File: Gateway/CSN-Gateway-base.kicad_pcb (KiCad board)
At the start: 2 copper layers, 32 x 85.5 mm, 51 parts, among them IC1 ATMEGA328-A, P2 CONN4, P3 CONN_ICSP, P5 CONN6, P8 CONN_NRF24L01, Q1 2N2222, U1 MAX485CSA, U2 AMS1117-3.3V, U3 ATSHA204A, Y1 Crystal

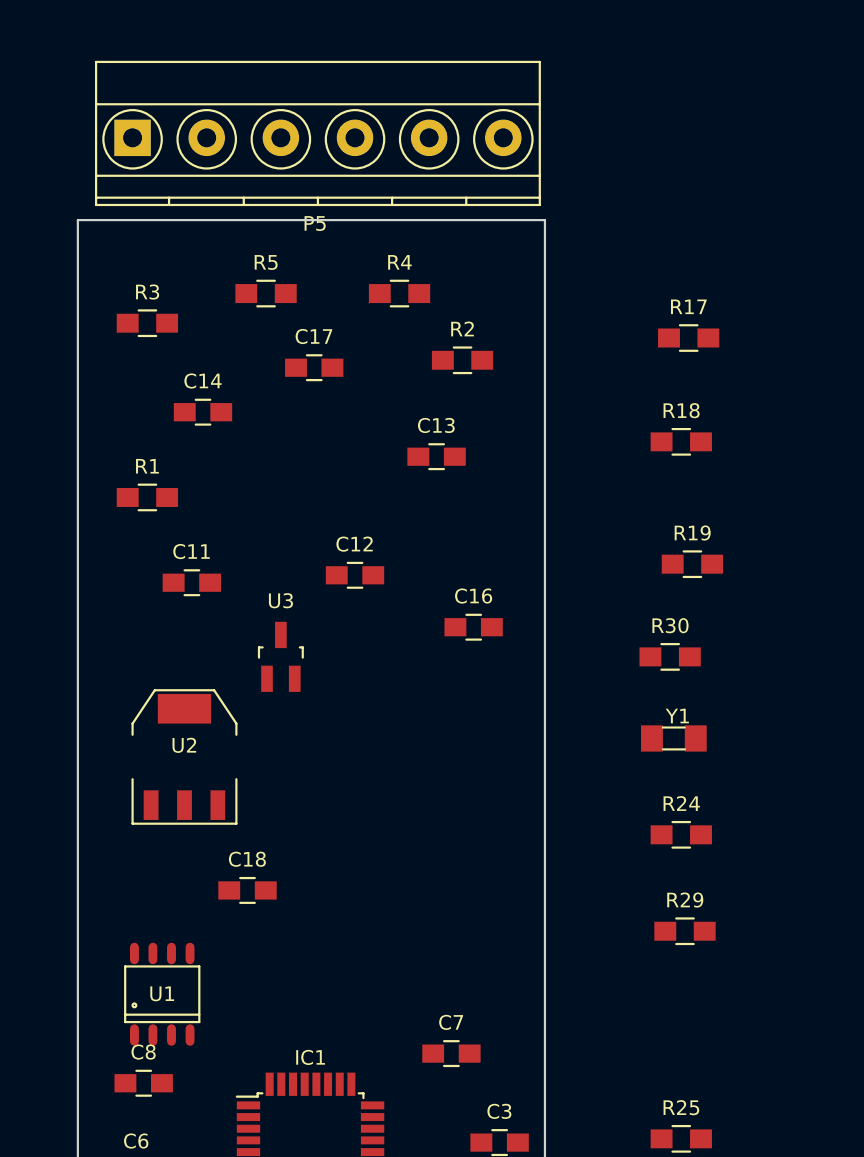
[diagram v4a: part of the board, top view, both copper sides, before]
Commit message: add all missing footprints
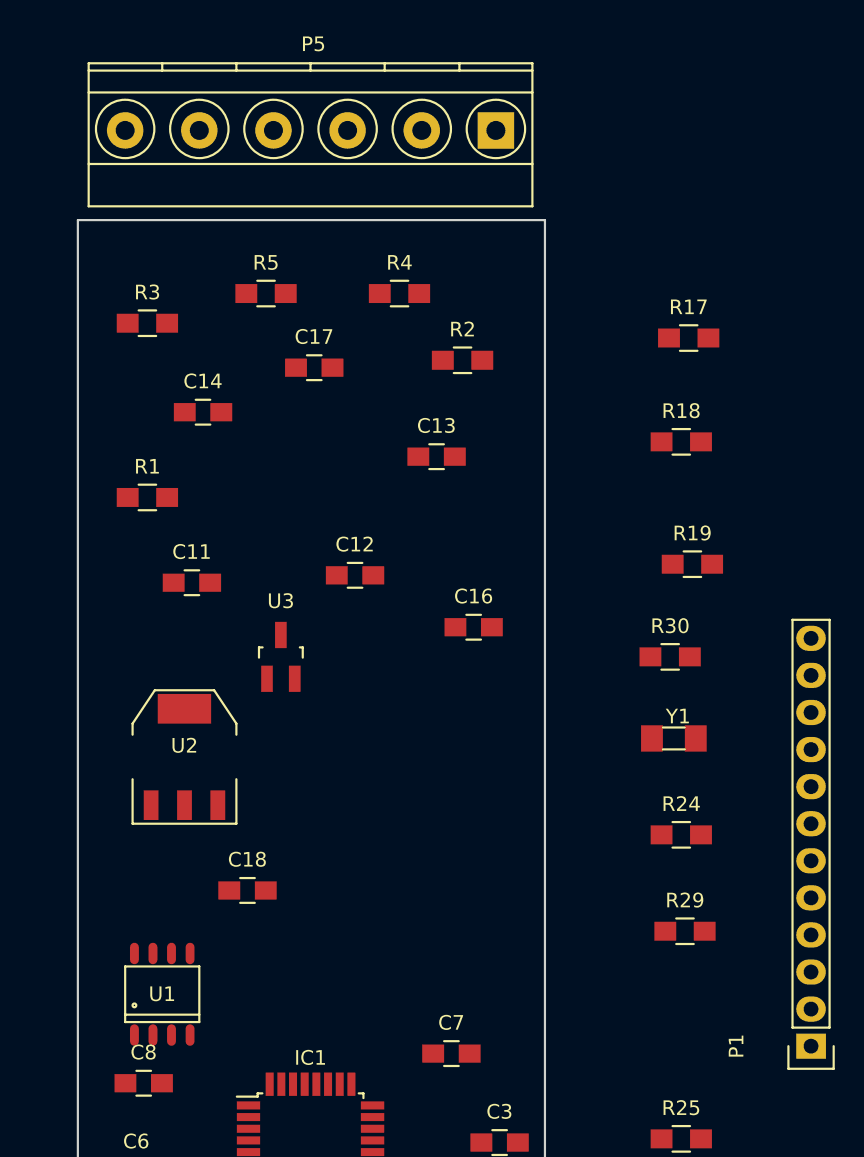
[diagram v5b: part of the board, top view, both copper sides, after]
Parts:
- added P1: CONN_02X06, Socket_Strips:Socket_Strip_Straight_1x12, F.Cu at (189.2, 117.1)
- moved P5 24.9 mm to (167.6, 54.4), turned to 180 degrees
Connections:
- IC1 pad 10: (no net) -> RGB2
- IC1 pad 11: (no net) -> RGB3
- IC1 pad 12: (no net) -> BTN1
- IC1 pad 25: (no net) -> BTN2
- IC1 pad 26: (no net) -> RGB1
- IC1 pad 28: (no net) -> SCL
- IC1 pad 30: (no net) -> RXI
- IC1 pad 31: (no net) -> TXO
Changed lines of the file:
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@@
 (kicad_pcb (version 4) (host pcbnew 4.0.4-stable)
   (general
-    (links 122)
-    (no_connects 122)
+    (links 134)
+    (no_connects 134)
     (area 138.924999 60.424999 171.075001 146.075001)
     (thickness 1.6)
@@
     (tracks 0)
     (zones 0)
-    (modules 51)
-    (nets 31)
+    (modules 52)
+    (nets 39)
   )
   (page A4)
@@
   (net 29 RS485-A)
   (net 30 RS485-B)
+  (net 31 RGB2)
+  (net 32 RGB3)
+  (net 33 BTN1)
+  (net 34 BTN2)
+  (net 35 RGB1)
+  (net 36 SCL)
+  (net 37 RXI)
+  (net 38 TXO)
   (net_class Default "Ceci est la Netclass par défaut"
     (clearance 0.2)
@@
     (add_net A2)
     (add_net A3)
+    (add_net BTN1)
+    (add_net BTN2)
     (add_net CE)
     (add_net CSN)
@@
     (add_net "Net-(D2-Pad1)")
     (add_net "Net-(P2-Pad2)")
+    (add_net RGB1)
+    (add_net RGB2)
+    (add_net RGB3)
     (add_net RS485-A)
     (add_net RS485-B)
@@
     (add_net RS485_TX)
     (add_net RST)
+    (add_net RXI)
     (add_net SCK)
+    (add_net SCL)
     (add_net SDA)
+    (add_net TXO)
     (add_net VCC)
   )
@@
     (pad 9 smd rect (at -2.8 4.25 90) (size 1.6 0.55) (layers F.Cu F.Paste F.Mask)
       (net 15 RS485_EN))
-    (pad 10 smd rect (at -2 4.25 90) (size 1.6 0.55) (layers F.Cu F.Paste F.Mask))
-    (pad 11 smd rect (at -1.2 4.25 90) (size 1.6 0.55) (layers F.Cu F.Paste F.Mask))
-    (pad 12 smd rect (at -0.4 4.25 90) (size 1.6 0.55) (layers F.Cu F.Paste F.Mask))
+    (pad 10 smd rect (at -2 4.25 90) (size 1.6 0.55) (layers F.Cu F.Paste F.Mask)
+      (net 31 RGB2))
+    (pad 11 smd rect (at -1.2 4.25 90) (size 1.6 0.55) (layers F.Cu F.Paste F.Mask)
+      (net 32 RGB3))
+    (pad 12 smd rect (at -0.4 4.25 90) (size 1.6 0.55) (layers F.Cu F.Paste F.Mask)
+      (net 33 BTN1))
     (pad 13 smd rect (at 0.4 4.25 90) (size 1.6 0.55) (layers F.Cu F.Paste F.Mask)
       (net 22 CE))
@@
     (pad 24 smd rect (at 4.25 -2.8) (size 1.6 0.55) (layers F.Cu F.Paste F.Mask)
       (net 18 A1))
-    (pad 25 smd rect (at 2.8 -4.25 90) (size 1.6 0.55) (layers F.Cu F.Paste F.Mask))
-    (pad 26 smd rect (at 2 -4.25 90) (size 1.6 0.55) (layers F.Cu F.Paste F.Mask))
+    (pad 25 smd rect (at 2.8 -4.25 90) (size 1.6 0.55) (layers F.Cu F.Paste F.Mask)
+      (net 34 BTN2))
+    (pad 26 smd rect (at 2 -4.25 90) (size 1.6 0.55) (layers F.Cu F.Paste F.Mask)
+      (net 35 RGB1))
     (pad 27 smd rect (at 1.2 -4.25 90) (size 1.6 0.55) (layers F.Cu F.Paste F.Mask)
       (net 19 SDA))
-    (pad 28 smd rect (at 0.4 -4.25 90) (size 1.6 0.55) (layers F.Cu F.Paste F.Mask))
+    (pad 28 smd rect (at 0.4 -4.25 90) (size 1.6 0.55) (layers F.Cu F.Paste F.Mask)
+      (net 36 SCL))
     (pad 29 smd rect (at -0.4 -4.25 90) (size 1.6 0.55) (layers F.Cu F.Paste F.Mask)
       (net 3 RST))
-    (pad 30 smd rect (at -1.2 -4.25 90) (size 1.6 0.55) (layers F.Cu F.Paste F.Mask))
-    (pad 31 smd rect (at -2 -4.25 90) (size 1.6 0.55) (layers F.Cu F.Paste F.Mask))
+    (pad 30 smd rect (at -1.2 -4.25 90) (size 1.6 0.55) (layers F.Cu F.Paste F.Mask)
+      (net 37 RXI))
+    (pad 31 smd rect (at -2 -4.25 90) (size 1.6 0.55) (layers F.Cu F.Paste F.Mask)
+      (net 38 TXO))
     (pad 32 smd rect (at -2.8 -4.25 90) (size 1.6 0.55) (layers F.Cu F.Paste F.Mask)
       (net 28 IRQ))
@@
   )
   (module footprints:TerminalBlock_Multicomp-5-08-6pol (layer F.Cu)
-    (at 142.748 54.864)
+    (at 167.64 54.356 180)
     (descr "6-way 5.08mm pitch terminal block, Multicomp MC000038")
-    (fp_text reference P5 (at 12.5 5.9) (layer F.SilkS)
-      (effects (font (size 1 1) (thickness 0.15)))
-    )
-    (fp_text value CONN6 (at 12.5 -6.6) (layer F.Fab)
+    (fp_text reference P5 (at 12.5 5.9 180) (layer F.SilkS)
+      (effects (font (size 1 1) (thickness 0.15)))
+    )
+    (fp_text value CONN6 (at 12.5 -6.6 180) (layer F.Fab)
       (effects (font (size 1 1) (thickness 0.15)))
     )
@@
     (fp_line (start 27.9 -5.2) (end -2.5 -5.2) (layer F.SilkS) (width 0.15))
     (fp_line (start -2.5 -5.2) (end -2.5 4.6) (layer F.SilkS) (width 0.15))
-    (pad 6 thru_hole circle (at 25.4 0) (size 2.5 2.5) (drill 1.3) (layers *.Cu *.Mask)
+    (pad 6 thru_hole circle (at 25.4 0 180) (size 2.5 2.5) (drill 1.3) (layers *.Cu *.Mask)
       (net 16 A2))
-    (pad 5 thru_hole circle (at 20.32 0) (size 2.5 2.5) (drill 1.3) (layers *.Cu *.Mask)
+    (pad 5 thru_hole circle (at 20.32 0 180) (size 2.5 2.5) (drill 1.3) (layers *.Cu *.Mask)
       (net 7 "Net-(C6-Pad1)"))
-    (pad 4 thru_hole circle (at 15.24 0) (size 2.5 2.5) (drill 1.3) (layers *.Cu *.Mask)
+    (pad 4 thru_hole circle (at 15.24 0 180) (size 2.5 2.5) (drill 1.3) (layers *.Cu *.Mask)
       (net 18 A1))
-    (pad 3 thru_hole circle (at 10.16 0) (size 2.5 2.5) (drill 1.3) (layers *.Cu *.Mask)
+    (pad 3 thru_hole circle (at 10.16 0 180) (size 2.5 2.5) (drill 1.3) (layers *.Cu *.Mask)
       (net 8 "Net-(C7-Pad1)"))
-    (pad 1 thru_hole rect (at 0 0) (size 2.5 2.5) (drill 1.3) (layers *.Cu *.Mask)
+    (pad 1 thru_hole rect (at 0 0 180) (size 2.5 2.5) (drill 1.3) (layers *.Cu *.Mask)
       (net 6 "Net-(C5-Pad1)"))
-    (pad 2 thru_hole circle (at 5.08 0) (size 2.5 2.5) (drill 1.3) (layers *.Cu *.Mask)
+    (pad 2 thru_hole circle (at 5.08 0 180) (size 2.5 2.5) (drill 1.3) (layers *.Cu *.Mask)
       (net 17 A0))
     (model Terminal_Blocks.3dshapes/TerminalBlock_Pheonix_MKDS1.5-6pol.wrl
@@
     )
   )
+  (module Socket_Strips:Socket_Strip_Straight_1x12 (layer F.Cu)
+    (at 189.23 117.094 90)
+    (descr "Through hole socket strip")
+    (tags "socket strip")
+    (fp_text reference P1 (at 0 -5.1 90) (layer F.SilkS)
+      (effects (font (size 1 1) (thickness 0.15)))
+    )
+    (fp_text value CONN_02X06 (at 0 -3.1 90) (layer F.Fab)
+      (effects (font (size 1 1) (thickness 0.15)))
+    )
+    (fp_line (start -1.75 -1.75) (end -1.75 1.75) (layer F.CrtYd) (width 0.05))
+    (fp_line (start 29.7 -1.75) (end 29.7 1.75) (layer F.CrtYd) (width 0.05))
+    (fp_line (start -1.75 -1.75) (end 29.7 -1.75) (layer F.CrtYd) (width 0.05))
+    (fp_line (start -1.75 1.75) (end 29.7 1.75) (layer F.CrtYd) (width 0.05))
+    (fp_line (start 1.27 1.27) (end 29.21 1.27) (layer F.SilkS) (width 0.15))
+    (fp_line (start 29.21 1.27) (end 29.21 -1.27) (layer F.SilkS) (width 0.15))
+    (fp_line (start 29.21 -1.27) (end 1.27 -1.27) (layer F.SilkS) (width 0.15))
+    (fp_line (start -1.55 1.55) (end 0 1.55) (layer F.SilkS) (width 0.15))
+    (fp_line (start 1.27 1.27) (end 1.27 -1.27) (layer F.SilkS) (width 0.15))
+    (fp_line (start 0 -1.55) (end -1.55 -1.55) (layer F.SilkS) (width 0.15))
+    (fp_line (start -1.55 -1.55) (end -1.55 1.55) (layer F.SilkS) (width 0.15))
+    (pad 1 thru_hole rect (at 0 0 90) (size 1.7272 2.032) (drill 1.016) (layers *.Cu *.Mask)
+      (net 9 VCC))
+    (pad 2 thru_hole oval (at 2.54 0 90) (size 1.7272 2.032) (drill 1.016) (layers *.Cu *.Mask)
+      (net 37 RXI))
+    (pad 3 thru_hole oval (at 5.08 0 90) (size 1.7272 2.032) (drill 1.016) (layers *.Cu *.Mask)
+      (net 2 GND))
+    (pad 4 thru_hole oval (at 7.62 0 90) (size 1.7272 2.032) (drill 1.016) (layers *.Cu *.Mask)
+      (net 38 TXO))
+    (pad 5 thru_hole oval (at 10.16 0 90) (size 1.7272 2.032) (drill 1.016) (layers *.Cu *.Mask)
+      (net 36 SCL))
+    (pad 6 thru_hole oval (at 12.7 0 90) (size 1.7272 2.032) (drill 1.016) (layers *.Cu *.Mask)
+      (net 3 RST))
+    (pad 7 thru_hole oval (at 15.24 0 90) (size 1.7272 2.032) (drill 1.016) (layers *.Cu *.Mask)
+      (net 19 SDA))
+    (pad 8 thru_hole oval (at 17.78 0 90) (size 1.7272 2.032) (drill 1.016) (layers *.Cu *.Mask)
+      (net 33 BTN1))
+    (pad 9 thru_hole oval (at 20.32 0 90) (size 1.7272 2.032) (drill 1.016) (layers *.Cu *.Mask)
+      (net 32 RGB3))
+    (pad 10 thru_hole oval (at 22.86 0 90) (size 1.7272 2.032) (drill 1.016) (layers *.Cu *.Mask)
+      (net 34 BTN2))
+    (pad 11 thru_hole oval (at 25.4 0 90) (size 1.7272 2.032) (drill 1.016) (layers *.Cu *.Mask)
+      (net 31 RGB2))
+    (pad 12 thru_hole oval (at 27.94 0 90) (size 1.7272 2.032) (drill 1.016) (layers *.Cu *.Mask)
+      (net 35 RGB1))
+    (model Socket_Strips.3dshapes/Socket_Strip_Straight_1x12.wrl
+      (at (xyz 0.55 0 0))
+      (scale (xyz 1 1 1))
+      (rotate (xyz 0 0 180))
+    )
+  )

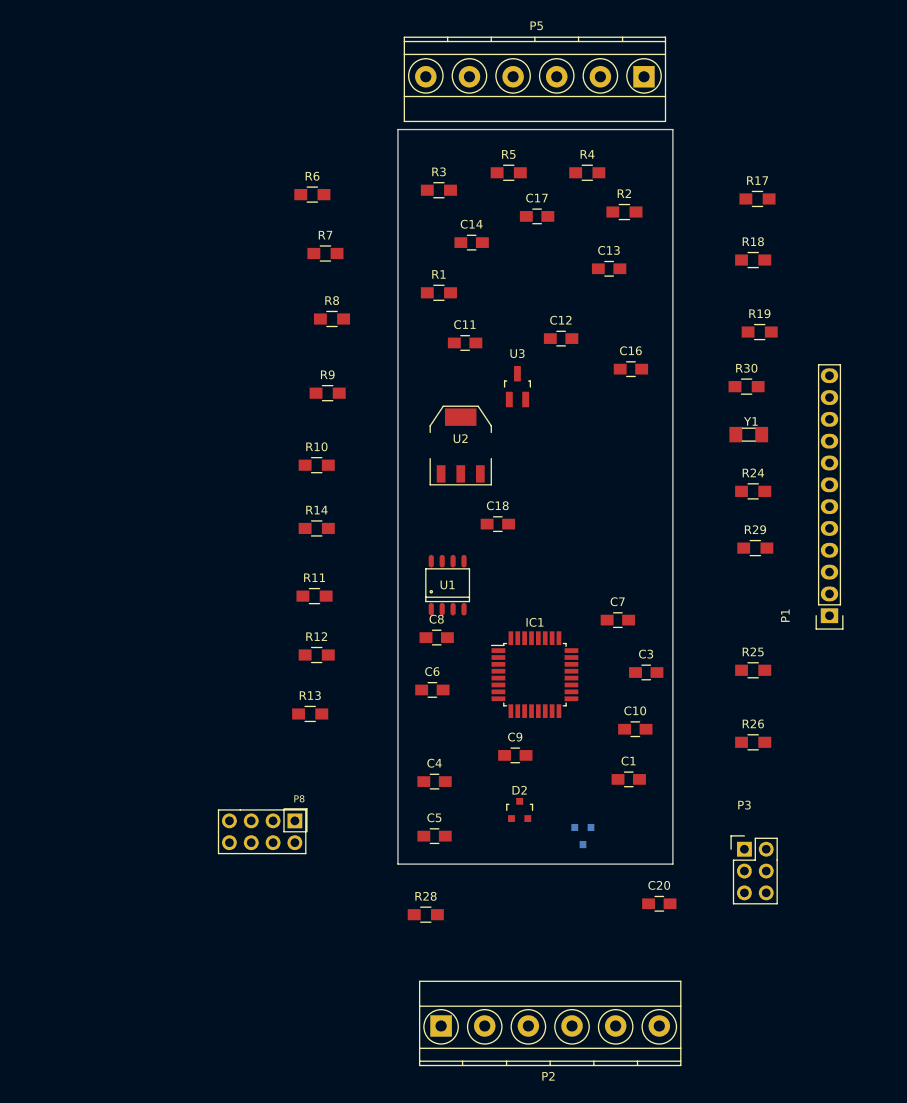
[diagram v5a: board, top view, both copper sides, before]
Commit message: begin placement of compo on base pcb
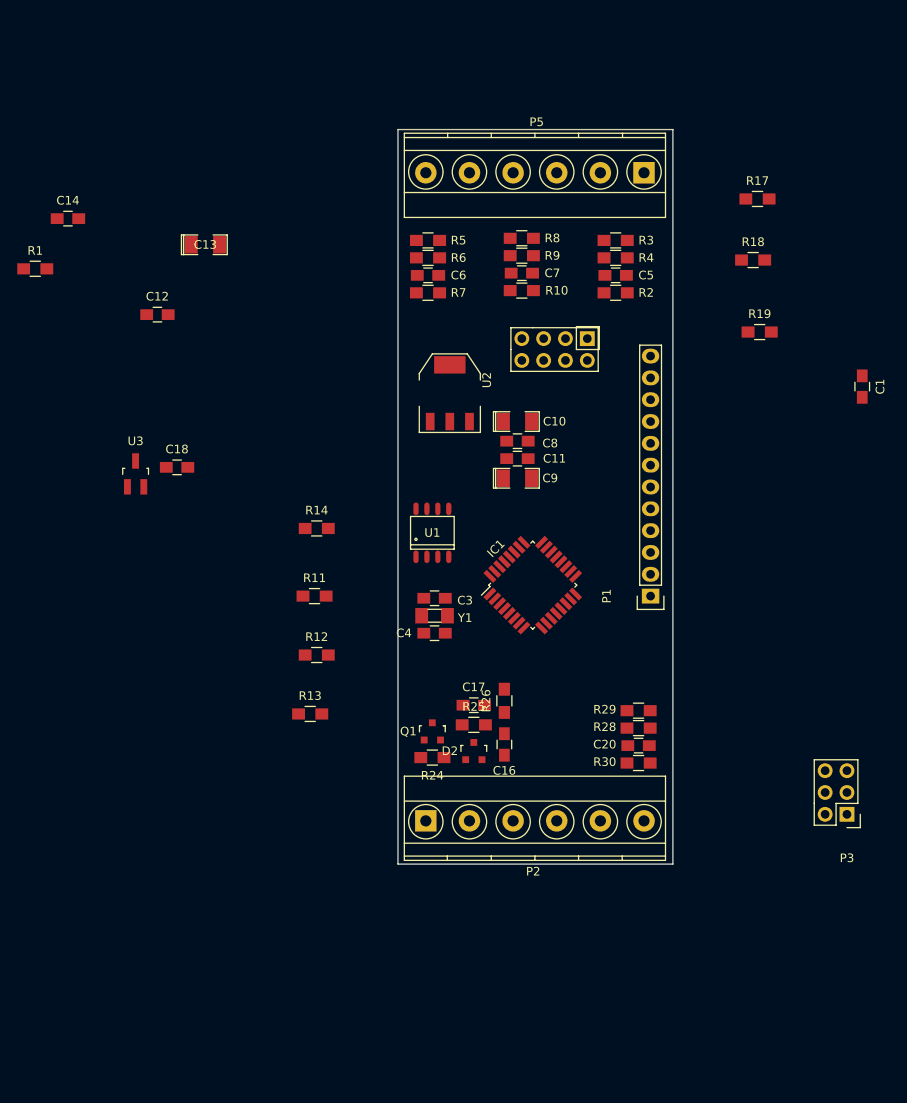
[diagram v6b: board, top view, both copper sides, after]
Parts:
- C10, C13, C9: footprint Capacitors_SMD:C_0805_HandSoldering -> SMD_Packages:SMD-1206_Pol
- Q1: moved to F.Cu
- moved C5 68.6 mm to (164.3, 77.5)
- moved P8 65.6 mm to (162.6, 83.3)
- moved C17 57.4 mm to (147.8, 127.5)
- moved C1 53.2 mm to (193.0, 90.4), turned to 270 degrees
- moved R24 48.5 mm to (143.0, 133.6), turned to 180 degrees
- moved C6 48.3 mm to (142.5, 77.5)
- moved C14 47.1 mm to (100.6, 70.9)
- moved R1 47.1 mm to (96.8, 76.7)
- moved C12 47.1 mm to (111.0, 82.0)
- moved C13 47.1 mm to (116.6, 73.9)
- moved C16 46.1 mm to (151.4, 132.1), turned to 270 degrees
- moved U3 45.6 mm to (108.5, 100.6)
- moved R30 45.6 mm to (167.0, 134.2), turned to 180 degrees
- moved Y1 42.2 mm to (143.3, 117.1)
- moved C7 41.9 mm to (153.4, 77.2)
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
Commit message: Finish base pcb routing and adjust all mounting holes
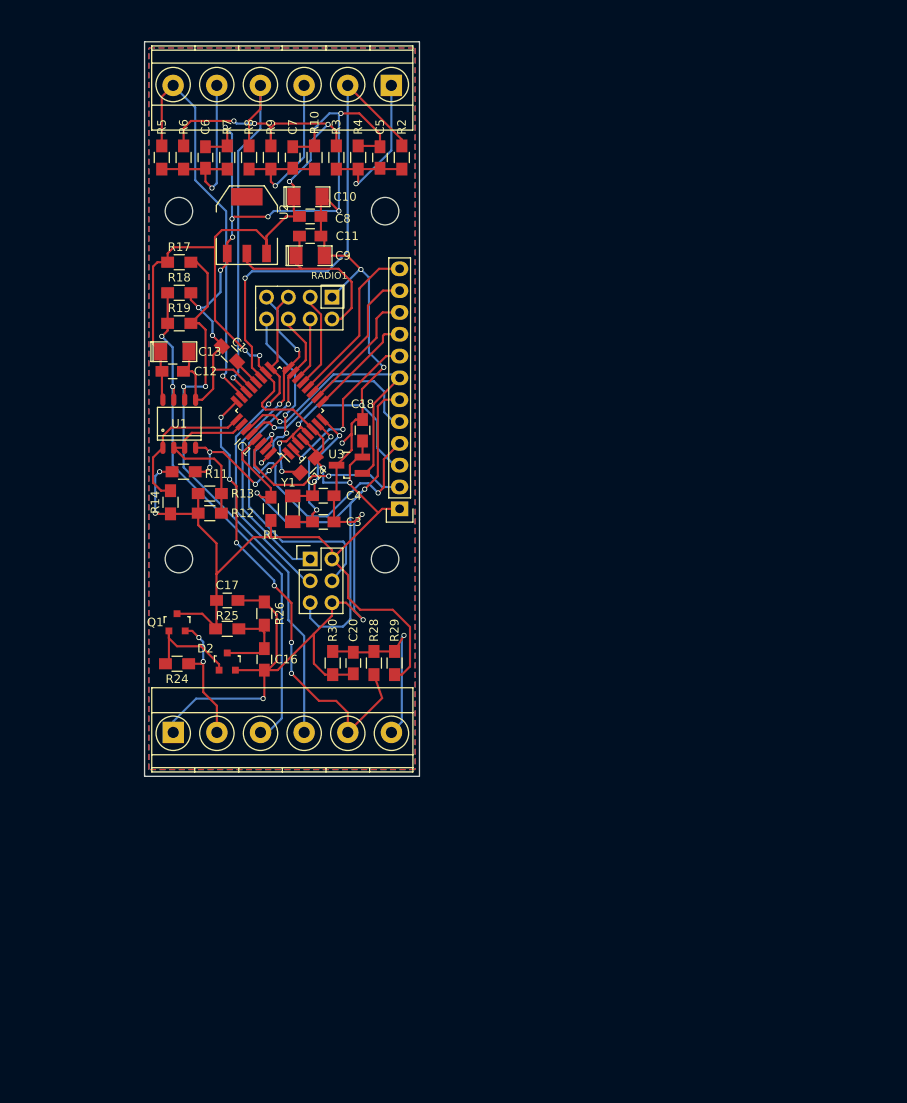
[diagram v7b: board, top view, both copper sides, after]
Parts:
- added ?: , Mounting_Holes:MountingHole_3.2mm_M3, F.Cu at (113.5, 110.5)
- added ?: , Mounting_Holes:MountingHole_3.2mm_M3, F.Cu at (137.5, 110.5)
- added ?: , Mounting_Holes:MountingHole_3.2mm_M3, F.Cu at (137.5, 70.0)
- added ?: , Mounting_Holes:MountingHole_3.2mm_M3, F.Cu at (113.5, 70.0)
- moved C1 73.8 mm to (119.4, 86.6), turned to 135 degrees
- moved P3 69.2 mm to (128.8, 110.5), turned to 0 degrees
- moved R17 67.7 mm to (113.5, 75.9)
- moved R19 67.6 mm to (113.5, 83.1)
- moved R18 66.9 mm to (113.5, 79.5)
- moved C14 40.1 mm to (128.5, 99.6), turned to 225 degrees
- moved R1 39.2 mm to (124.2, 104.6), turned to 90 degrees
- moved R30 37.5 mm to (131.4, 122.6), turned to 270 degrees
- moved IC1 35.8 mm to (125.2, 93.2), turned to 135 degrees
- moved C10 35.8 mm to (128.5, 68.3)
- moved C8 35.6 mm to (128.8, 70.6)
- moved C11 35.4 mm to (128.8, 72.9)
- moved C9 35.4 mm to (128.8, 75.2)
- moved C20 34.6 mm to (133.8, 122.6), turned to 270 degrees
- moved R3 33.9 mm to (131.8, 63.8), turned to 90 degrees
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- renumbered P8 to RADIO1
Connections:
- IC1 pad 10: RGB2 -> BTN2
- IC1 pad 11: RGB3 -> RGB2
- IC1 pad 12: BTN1 -> RGB1
- IC1 pad 19: A2 -> A0
- IC1 pad 2: RS485_TX -> BTN1
- IC1 pad 22: A3 -> A1
- IC1 pad 23: A0 -> A2
- IC1 pad 24: A1 -> A3
- IC1 pad 25: BTN2 -> RS485_TX
- IC1 pad 26: RGB1 -> RS485_EN
- IC1 pad 9: RS485_EN -> RGB3
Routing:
- net GND: track 0.00 -> 257.6 mm, vias 0 -> 20
- net VCC: track 0.00 -> 219.0 mm, vias 0 -> 10
- net RS485-A: track 0.00 -> 68.6 mm, vias 0 -> 2
- net RST: track 0.00 -> 62.4 mm, vias 0 -> 2
- net RS485-B: track 0.00 -> 60.3 mm, vias 0 -> 2
- net A3: track 0.00 -> 55.2 mm, vias 0 -> 6
- net A0: track 0.00 -> 54.8 mm, vias 0 -> 1
- net A2: track 0.00 -> 47.5 mm, vias 0 -> 1
- net A1: track 0.00 -> 46.5 mm, vias 0 -> 1
- net MOSI: track 0.00 -> 43.4 mm, vias 0 -> 1
- net SCK: track 0.00 -> 40.3 mm, vias 0 -> 1
- net MISO: track 0.00 -> 39.5 mm, vias 0 -> 2
- net SDA: track 0.00 -> 35.1 mm, vias 0 -> 1
- net TXO: track 0.00 -> 34.6 mm, vias 0 -> 2
- net Net-(C6-Pad1): track 0.00 -> 27.5 mm, vias 0 -> 1
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- added copper zone on B.Cu, net GND
- added copper zone on F.Cu, net GND
